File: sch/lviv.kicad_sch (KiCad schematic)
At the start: 0 parts

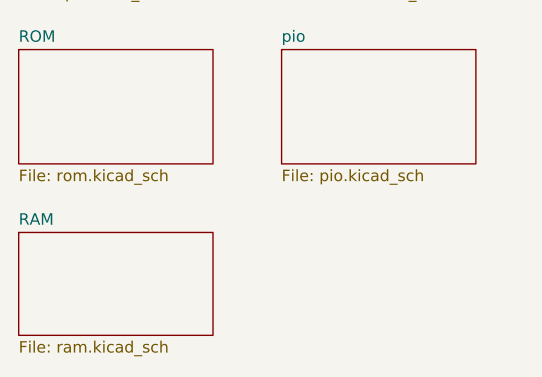
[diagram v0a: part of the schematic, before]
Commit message: Sch: started timing block
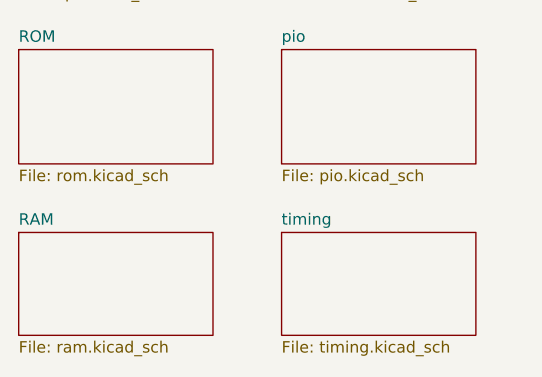
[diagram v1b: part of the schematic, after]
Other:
- added sheet timing (timing.kicad_sch)
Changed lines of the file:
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@@
+    )
+  )
+  (sheet (at 73.66 69.85) (size 21.59 11.43) (fields_autoplaced)
+    (stroke (width 0.1524) (type solid) (color 0 0 0 0))
+    (fill (color 0 0 0 0.0000))
+    (property "Sheet name" "timing" (id 0) (at 73.66 69.1384 0)
+      (effects (font (size 1.27 1.27)) (justify left bottom))
+    )
+    (property "Sheet file" "timing.kicad_sch" (id 1) (at 73.66 81.8646 0)
+      (effects (font (size 1.27 1.27)) (justify left top))
     )
   )
@@
     (path "/036afffe-cbbf-4ead-9c0c-ea4c435dd04c" (page "5"))
     (path "/bc747cd9-2c14-4e8d-af52-0eda425fcd05" (page "6"))
+    (path "/b85f8c73-19f2-44f2-9443-5936ad5dc890" (page "7"))
   )
   (symbol_instances
@@
       (reference "#PWR?") (unit 1) (value "+5V") (footprint "")
     )
+    (path "/b85f8c73-19f2-44f2-9443-5936ad5dc890/4b187bec-4ed4-4b48-8432-9f5372e327d3"
+      (reference "#PWR?") (unit 1) (value "GND") (footprint "")
+    )
     (path "/036afffe-cbbf-4ead-9c0c-ea4c435dd04c/4b5ea97b-e6aa-4fa8-ae11-6542bd1bd454"
       (reference "#PWR?") (unit 1) (value "+5V") (footprint "")
@@
       (reference "#PWR?") (unit 1) (value "+5V") (footprint "")
     )
+    (path "/b85f8c73-19f2-44f2-9443-5936ad5dc890/6615abd6-1793-4cc0-87f1-78313216f32f"
+      (reference "#PWR?") (unit 1) (value "GND") (footprint "")
+    )
     (path "/bc747cd9-2c14-4e8d-af52-0eda425fcd05/6ddf1a43-d073-4405-ad4f-9cc4c97fd3f2"
       (reference "#PWR?") (unit 1) (value "GND") (footprint "")
@@
       (reference "#PWR?") (unit 1) (value "+5V") (footprint "")
     )
+    (path "/b85f8c73-19f2-44f2-9443-5936ad5dc890/762f8e71-8801-4603-928e-99e837cab0ad"
+      (reference "#PWR?") (unit 1) (value "GND") (footprint "")
+    )
     (path "/e9506136-80e5-4250-83e4-52799f917e83/7802567c-2c46-42ef-ba45-d2f84fc9caf4"
       (reference "#PWR?") (unit 1) (value "+5V") (footprint "")
@@
     (path "/e9506136-80e5-4250-83e4-52799f917e83/e6a5310e-f445-408c-870f-3c30ce286407"
       (reference "#PWR?") (unit 1) (value "GND") (footprint "")
+    )
+    (path "/b85f8c73-19f2-44f2-9443-5936ad5dc890/ef4842f6-f650-4ba8-bb24-b40cfb06d1eb"
+      (reference "#PWR?") (unit 1) (value "+5V") (footprint "")
     )
     (path "/39367e70-4fd8-4578-b7c9-16f6f15e83e4/ef6c14c2-90f4-4268-be66-9d8ac087276f"
@@
       (reference "D32") (unit 1) (value "8226") (footprint "")
     )
+    (path "/b85f8c73-19f2-44f2-9443-5936ad5dc890/43729c41-452a-4601-b7e4-6f7f1f23761d"
+      (reference "D33") (unit 1) (value "74S04") (footprint "")
+    )
+    (path "/b85f8c73-19f2-44f2-9443-5936ad5dc890/45b11813-3c13-4838-a829-e1eb453eb6fd"
+      (reference "D34") (unit 1) (value "74LS193") (footprint "")
+    )
+    (path "/b85f8c73-19f2-44f2-9443-5936ad5dc890/b0c82337-8700-4eca-8511-987c30d9bc03"
+      (reference "D35") (unit 1) (value "74LS193") (footprint "")
+    )
+    (path "/b85f8c73-19f2-44f2-9443-5936ad5dc890/0c956d82-fdad-4ad9-b7e9-6a7255a57e4d"
+      (reference "D36") (unit 1) (value "74LS93") (footprint "")
+    )
     (path "/e9506136-80e5-4250-83e4-52799f917e83/724eeae1-01bb-4e26-bed2-a801c6b1e80a"
       (reference "D51") (unit 1) (value "74LS153") (footprint "")
@@
       (reference "R28") (unit 1) (value "~") (footprint "")
     )
+    (path "/b85f8c73-19f2-44f2-9443-5936ad5dc890/626660d4-67c1-4532-8180-8968c817c64e"
+      (reference "R29") (unit 1) (value "R") (footprint "")
+    )
     (path "/e9506136-80e5-4250-83e4-52799f917e83/46d384a7-c731-4819-92b8-fc60ac2100f5"
       (reference "R30") (unit 1) (value "R_Small") (footprint "")
@@
       (reference "R33") (unit 1) (value "~") (footprint "")
     )
-    (path "/e9506136-80e5-4250-83e4-52799f917e83/ff534714-5450-4ad6-a07c-a8ccad3be11b"
+    (path "/e9506136-80e5-4250-83e4-52799f917e83/ff534714-5450-4ad6-a07c-a8ccad3be11c"
       (reference "R34") (unit 1) (value "R_Small") (footprint "")
     )

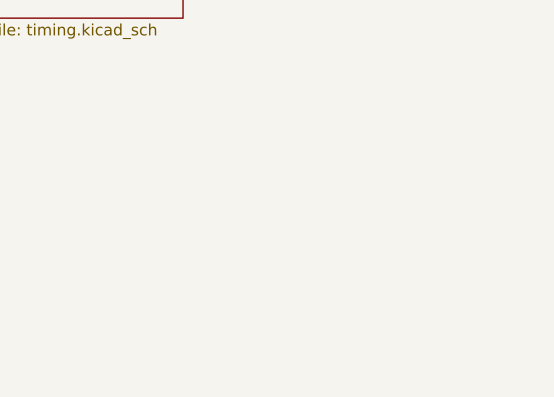
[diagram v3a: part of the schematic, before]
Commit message: Extracted RAM controller
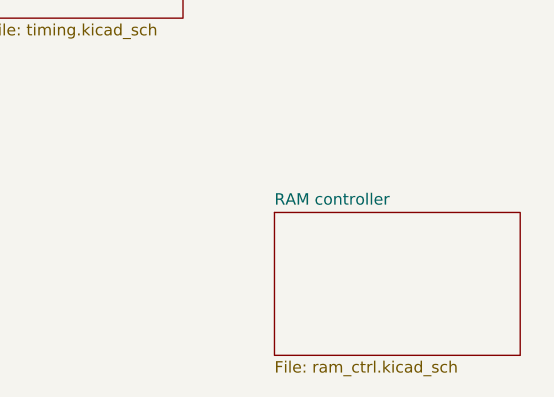
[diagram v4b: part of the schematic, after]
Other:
- added sheet RAM controller (ram_ctrl.kicad_sch)

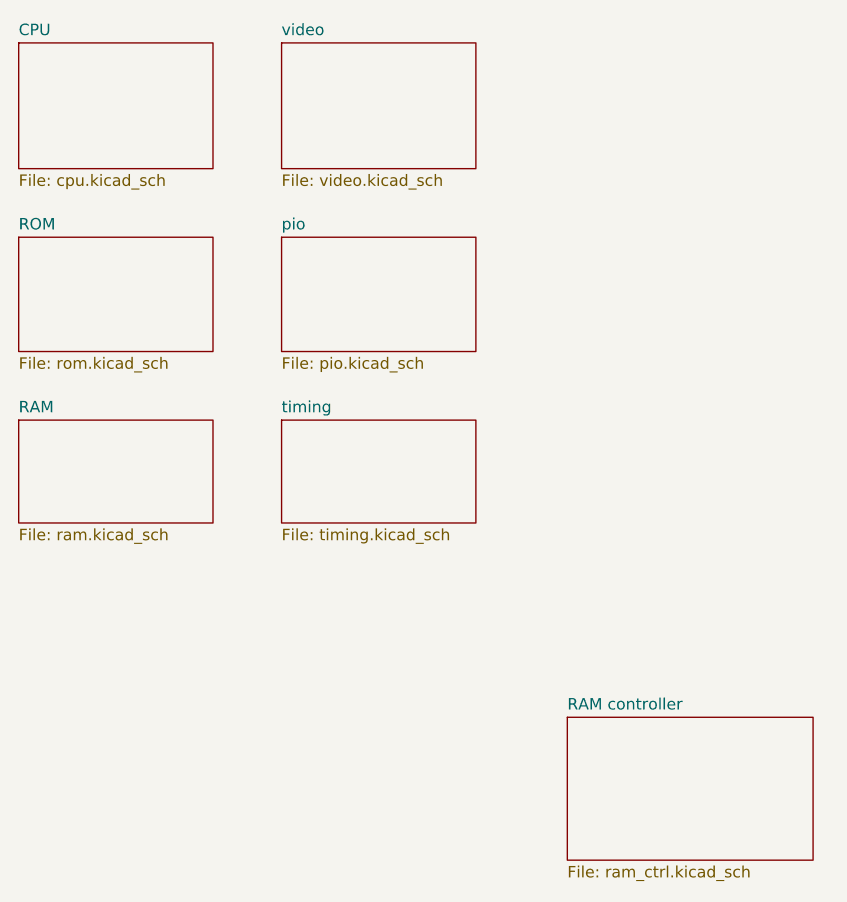
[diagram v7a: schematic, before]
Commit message: Sch: mem remapping circuit moved to ROM sheet
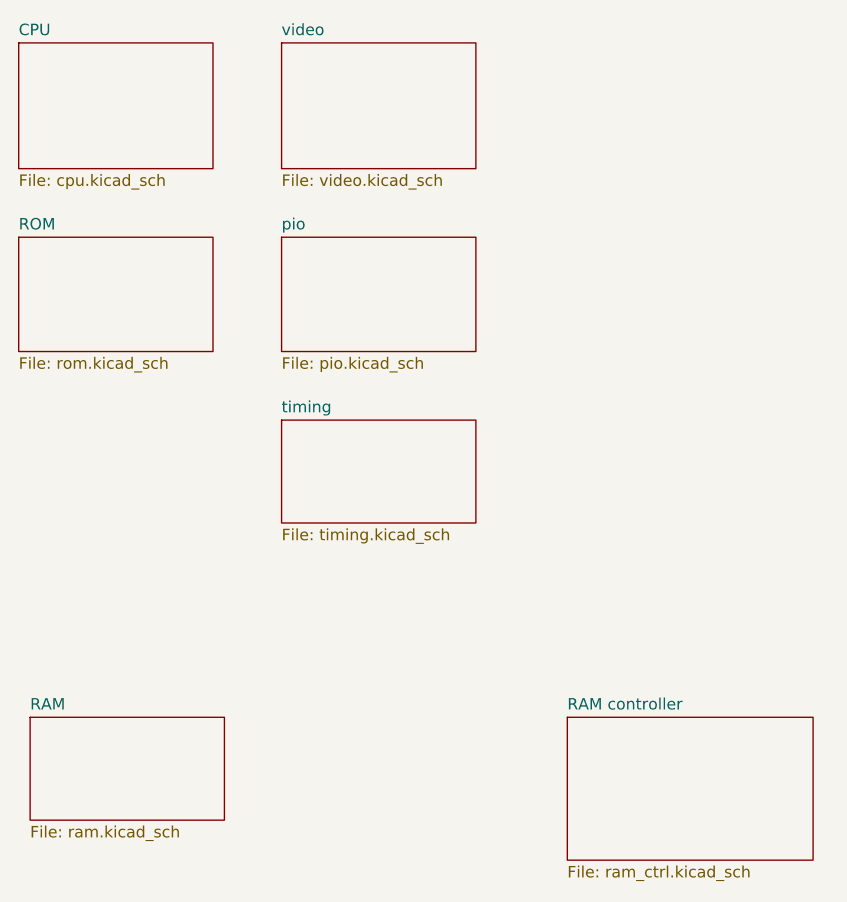
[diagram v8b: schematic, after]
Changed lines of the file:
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@@
     )
   )
-  (sheet (at 44.45 69.85) (size 21.59 11.43) (fields_autoplaced)
+  (sheet (at 45.72 102.87) (size 21.59 11.43) (fields_autoplaced)
     (stroke (width 0.1524) (type solid) (color 0 0 0 0))
     (fill (color 0 0 0 0.0000))
-    (property "Sheet name" "RAM" (id 0) (at 44.45 69.1384 0)
+    (property "Sheet name" "RAM" (id 0) (at 45.72 102.1584 0)
       (effects (font (size 1.27 1.27)) (justify left bottom))
     )
-    (property "Sheet file" "ram.kicad_sch" (id 1) (at 44.45 81.8646 0)
+    (property "Sheet file" "ram.kicad_sch" (id 1) (at 45.72 114.8846 0)
       (effects (font (size 1.27 1.27)) (justify left top))
     )
@@
       (reference "#PWR?") (unit 1) (value "GND") (footprint "")
     )
+    (path "/39367e70-4fd8-4578-b7c9-16f6f15e83e4/542b7669-e996-4107-b9de-31591867d2a3"
+      (reference "#PWR?") (unit 1) (value "GND") (footprint "")
+    )
     (path "/e9506136-80e5-4250-83e4-52799f917e83/5b4a0958-4431-48ba-8cba-216fe96b76a1"
       (reference "#PWR?") (unit 1) (value "GND") (footprint "")
@@
     (path "/39367e70-4fd8-4578-b7c9-16f6f15e83e4/c26a68d2-a29a-4992-8792-62929ff7fbe7"
       (reference "#PWR?") (unit 1) (value "~") (footprint "")
-    )
-    (path "/ec5c2062-3a41-4636-8803-069e60a1641a/c4a3435a-68a1-4d1f-937e-dd4fd074efff"
-      (reference "#PWR?") (unit 1) (value "GND") (footprint "")
     )
     (path "/bc747cd9-2c14-4e8d-af52-0eda425fcd05/c8cfbe4e-05f1-4f17-a10f-e8b6945171a4"
@@
       (reference "C56") (unit 1) (value "C_Small") (footprint "")
     )
-    (path "/ec5c2062-3a41-4636-8803-069e60a1641a/a42762ae-33b2-425d-aa2c-10445b69f1d9"
+    (path "/39367e70-4fd8-4578-b7c9-16f6f15e83e4/c097debe-e454-4251-b206-03e8af27b926"
       (reference "D1") (unit 1) (value "7410") (footprint "")
     )
-    (path "/ec5c2062-3a41-4636-8803-069e60a1641a/303f88f9-98f1-43d7-bc94-fa291d73b511"
+    (path "/39367e70-4fd8-4578-b7c9-16f6f15e83e4/24985ab4-c2ca-46ee-bd16-3deea12c538b"
       (reference "D1") (unit 2) (value "7410") (footprint "")
     )
     (path "/ec5c2062-3a41-4636-8803-069e60a1641a/caebc74e-3b13-491e-a739-5835ef223ac6"
-      (reference "D2") (unit 1) (value "8286 / КР580ВА86") (footprint "")
+      (reference "D2") (unit 1) (value "8286") (footprint "")
     )
     (path "/ec5c2062-3a41-4636-8803-069e60a1641a/9c6e6373-02e6-4a50-bbfb-f7d763db156a"
-      (reference "D3") (unit 1) (value "8286 / КР580ВА86") (footprint "")
+      (reference "D3") (unit 1) (value "8286") (footprint "")
     )
     (path "/ec5c2062-3a41-4636-8803-069e60a1641a/59b21f1a-4908-44f3-b1d8-8559abe21d1e"
-      (reference "D4") (unit 1) (value "8224 / КР580ГФ24") (footprint "")
-    )
-    (path "/ec5c2062-3a41-4636-8803-069e60a1641a/af49318e-88f4-45de-92e0-89cce36323dd"
+      (reference "D4") (unit 1) (value "8224") (footprint "")
+    )
+    (path "/39367e70-4fd8-4578-b7c9-16f6f15e83e4/32ac19ea-f738-442b-afd8-52db5695980b"
       (reference "D5") (unit 1) (value "74LS74") (footprint "")
     )
     (path "/ec5c2062-3a41-4636-8803-069e60a1641a/becc5b0d-0352-4ad7-ac5e-da033ca0b239"
-      (reference "D6") (unit 1) (value "8080 / КР580ВМ80") (footprint "")
-    )
-    (path "/ec5c2062-3a41-4636-8803-069e60a1641a/ecb9382e-8212-4cf7-b9a3-cf1f144d2ec8"
+      (reference "D6") (unit 1) (value "8080") (footprint "")
+    )
+    (path "/39367e70-4fd8-4578-b7c9-16f6f15e83e4/32a9df2f-17cc-4454-b6f1-4c632b199b67"
       (reference "D7") (unit 2) (value "7408") (footprint "")
     )
     (path "/ec5c2062-3a41-4636-8803-069e60a1641a/71507327-aca7-400b-91af-35ed0f809b8f"
-      (reference "D8") (unit 1) (value "8228 / КР580ВК28") (footprint "")
+      (reference "D8") (unit 1) (value "8228") (footprint "")
     )
     (path "/39367e70-4fd8-4578-b7c9-16f6f15e83e4/448c97d9-acbf-4cb6-b6cc-530549ead6d1"
